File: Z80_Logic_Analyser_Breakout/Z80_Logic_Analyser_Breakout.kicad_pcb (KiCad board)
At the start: 2 copper layers, 40 x 53 mm, 4 parts, among them J1 Logic Analyser #1, J2 Z80 Socket, J3 Logic Analyser #2, U1 Z80 CPU

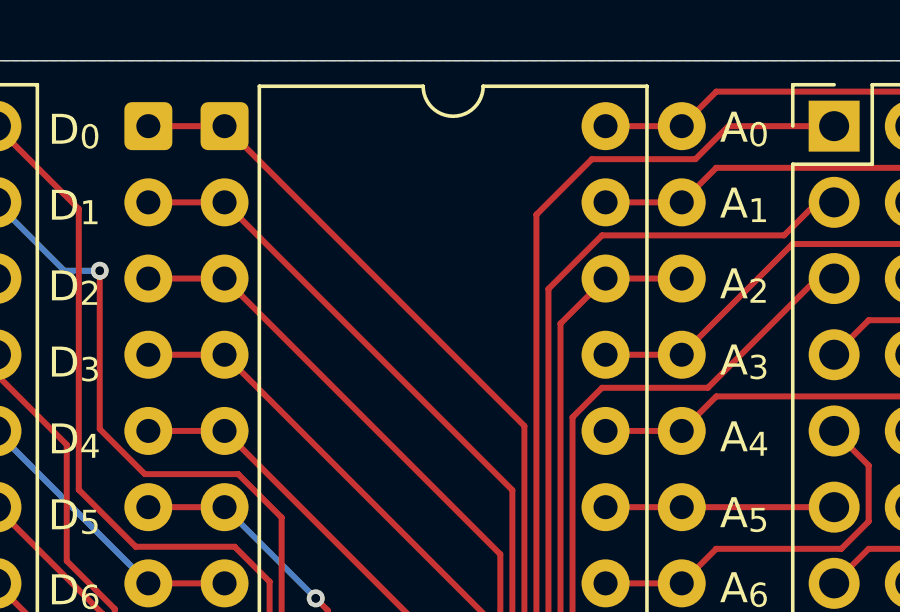
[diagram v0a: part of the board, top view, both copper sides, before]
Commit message: Cosmetic PCB change
And saved with KiCad 10 (sorry KiCad 9 users)
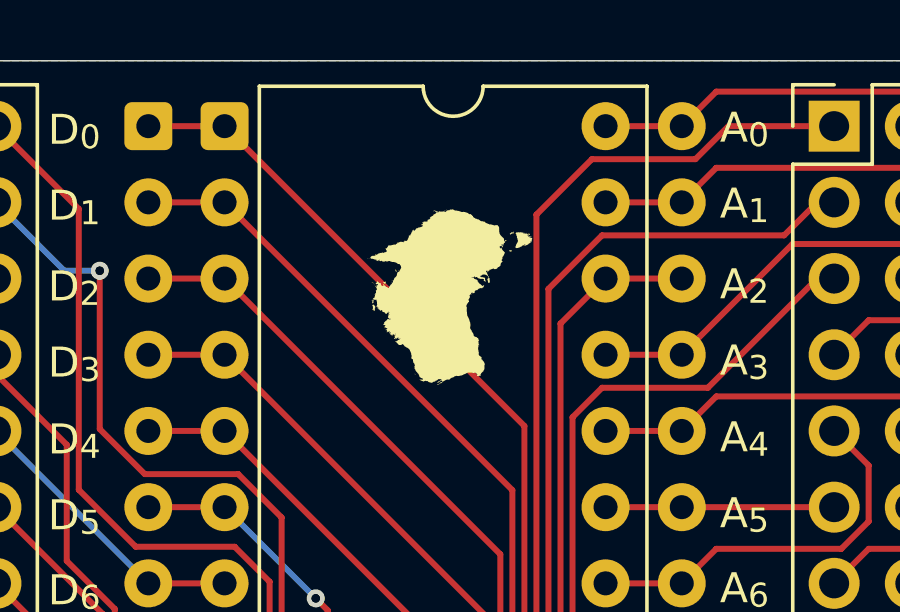
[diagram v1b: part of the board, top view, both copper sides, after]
